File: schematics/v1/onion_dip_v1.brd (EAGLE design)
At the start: 41 x 50 mm, 28 parts

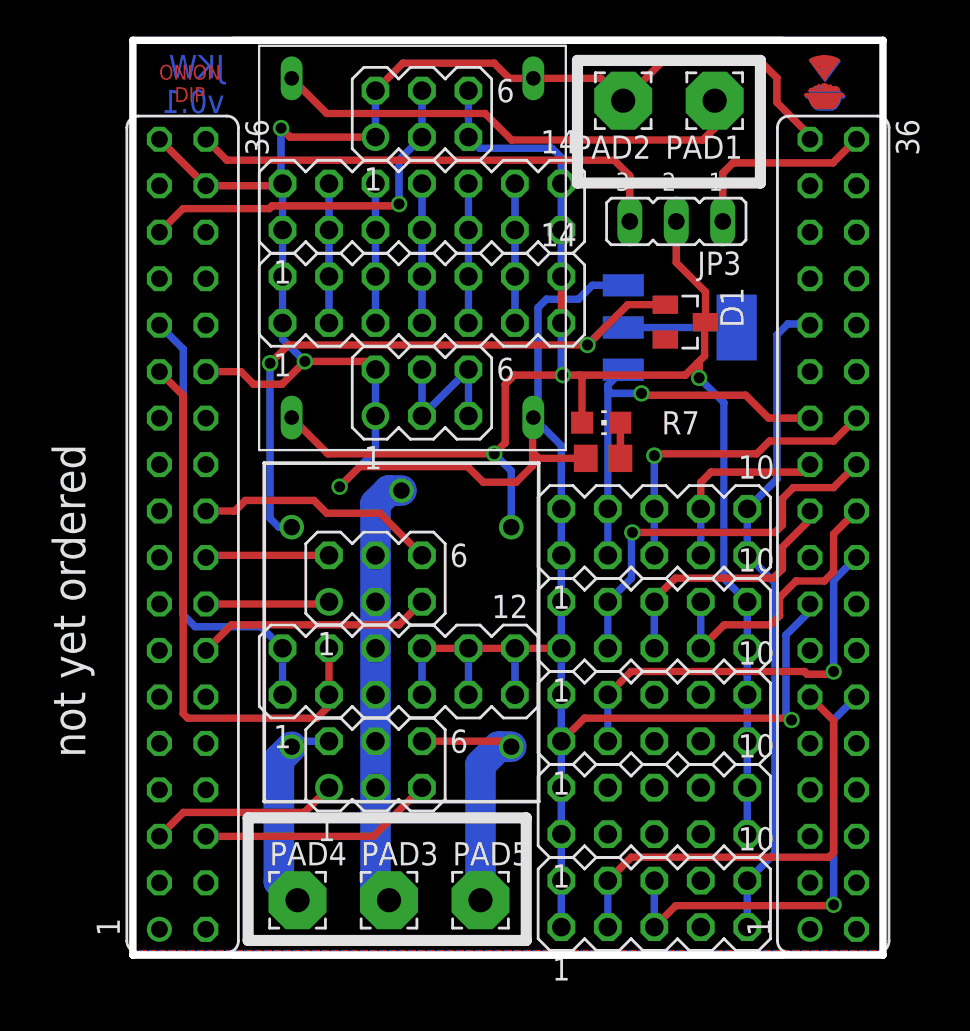
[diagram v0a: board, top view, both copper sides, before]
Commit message: added EEPROM, SPI, SMB Diode
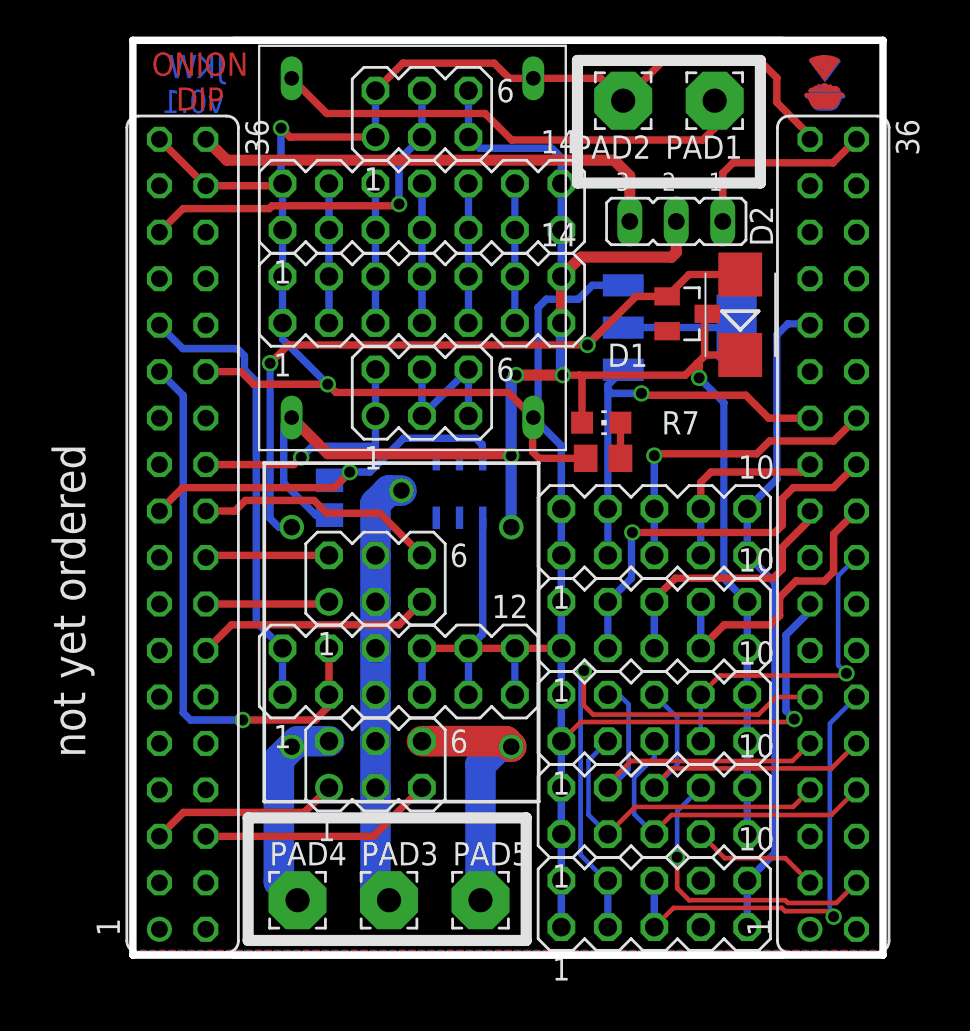
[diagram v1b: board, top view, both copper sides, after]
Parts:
- added D2: (no value), diode:SMB
- added IC2: DS2432P, 1wire:TSOC6
- added R1: (no value), rcl:R0805
- moved D1 0.46 mm to (30.3, 35.0)
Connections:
- removed net N$18: SV9.6
- removed net N$19: SV9.8
- removed net N$21: SV9.5
- removed net N$22: SV9.7
- removed net N$23: SV4.4
- removed net N$24: SV4.6
- removed net N$25: SV4.8
- removed net N$26: SV4.3
- removed net N$31: SV4.5
- removed net N$32: SV4.7
- net CSICK: now also SV4.6, SV9.6
- net CSIHSYNC: now also SV4.3, SV9.3
- net CSIPCK: now also SV4.4, SV9.4
- net CSVSYNC: now also SV4.5, SV9.5
- net D2: now also SV4.7
- net D3: now also SV4.8
- net GND: now also IC2.4; no longer SV15.1, SV15.2
- net LD2: now also IC2.3, R1.1
- net N$1: now also D2.A
- net P7: now also SV9.7, SV9.8; no longer SV9.3, SV9.4
- net VCC: now also D2.C, R1.2
- net Y2: now also SV15.1, SV15.2
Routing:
- net LD2: track 0.00 -> 21.5 mm, vias 0 -> 1
- net CSIPCK: track 0.00 -> 19.1 mm
- net CSICK: track 0.00 -> 18.2 mm
- net CSVSYNC: track 0.00 -> 18.1 mm
- net CSIHSYNC: track 0.00 -> 18.0 mm
- net D3: track 0.00 -> 16.6 mm, vias 0 -> 1
- net Y2: track 0.00 -> 13.9 mm, vias 0 -> 1
- net VCC: track 89.8 -> 101.4 mm, vias 3 -> 4
- net D2: track 0.00 -> 7.07 mm
- net SDA2: track 24.6 -> 29.7 mm, vias 0 -> 1
- net N$1: track 41.3 -> 46.1 mm
- net P7: track 22.3 -> 17.9 mm
- net GND: track 167.8 -> 166.1 mm, vias 4 -> 3
- net SCL2: track 24.7 -> 25.7 mm
- net SCK: track 30.7 -> 30.8 mm, vias 0 -> 1

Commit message: added UART header
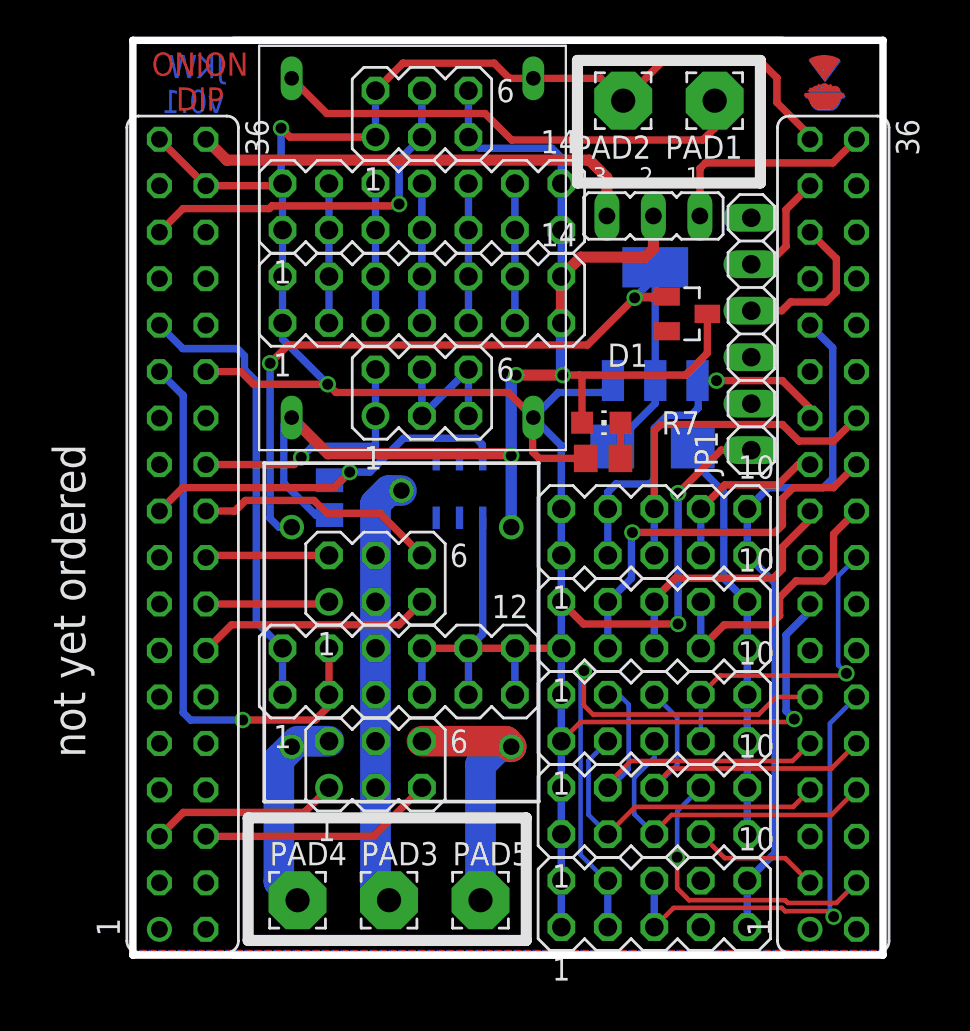
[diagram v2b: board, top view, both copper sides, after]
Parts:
- added JP1: (no value), pinhead:1X06
- moved D2 8.65 mm to (28.4, 27.8), flipped to the bottom, turned to 0 degrees
- moved U$3 1.36 mm to (28.6, 34.5), turned to 0 degrees
- moved JP3 1.29 mm to (28.4, 40.4)
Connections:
- net GND: now also JP1.1
- net RX: now also JP1.4
- net TX: now also JP1.5
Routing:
- net GND: track 166.1 -> 179.1 mm, vias 3 -> 5
- net RX: track 0.00 -> 8.93 mm
- net VCC: track 101.4 -> 94.9 mm, vias 4 -> 3
- net TX: track 0.00 -> 6.15 mm
- net _3V3: track 36.4 -> 38.4 mm
- net CHR_IN: track 26.5 -> 24.9 mm
- net P1: track 17.3 -> 18.9 mm, vias 1 -> 0
- net CHIP_5V: track 10.7 -> 12.2 mm
- net P0: track 22.2 -> 20.8 mm
- net N$1: track 46.1 -> 47.0 mm
- net P2: track 10.4 -> 9.51 mm

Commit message: new logo
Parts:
- removed U$2, U$5: LOGO, logo:LOGO
- added U$4, U$6: LOGO_3X3_COPPER, logo:LOGO_3X3_COPPER
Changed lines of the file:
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@@
 <attribute name="VALUE" x="42.979" y="0.14" size="1.27" layer="27" ratio="10" rot="R90"/>
 </element>
-<element name="U$2" library="logo" package="LOGO" value="LOGO" x="36.5379" y="46.0248"/>
-<element name="U$5" library="logo" package="LOGO" value="LOGO" x="39.0906" y="46.101" rot="MR0"/>
 <element name="PAD1" library="wirepad" package="3,17/1,3" value="WIREPAD3,17/1,3" x="31.8" y="46.7" rot="R180"/>
 <element name="PAD2" library="wirepad" package="3,17/1,3" value="WIREPAD3,17/1,3" x="26.8" y="46.7" rot="R180"/>
@@
 </element>
 <element name="JP1" library="pinhead" package="1X06" value="" x="33.8" y="33.95" rot="R90"/>
+<element name="U$4" library="logo" package="LOGO_3X3_COPPER" value="LOGO_3X3_COPPER" x="38.05" y="47.85"/>
+<element name="U$6" library="logo" package="LOGO_3X3_COPPER" value="LOGO_3X3_COPPER" x="38.05" y="47.85" rot="MR0"/>
 </elements>
 <signals>

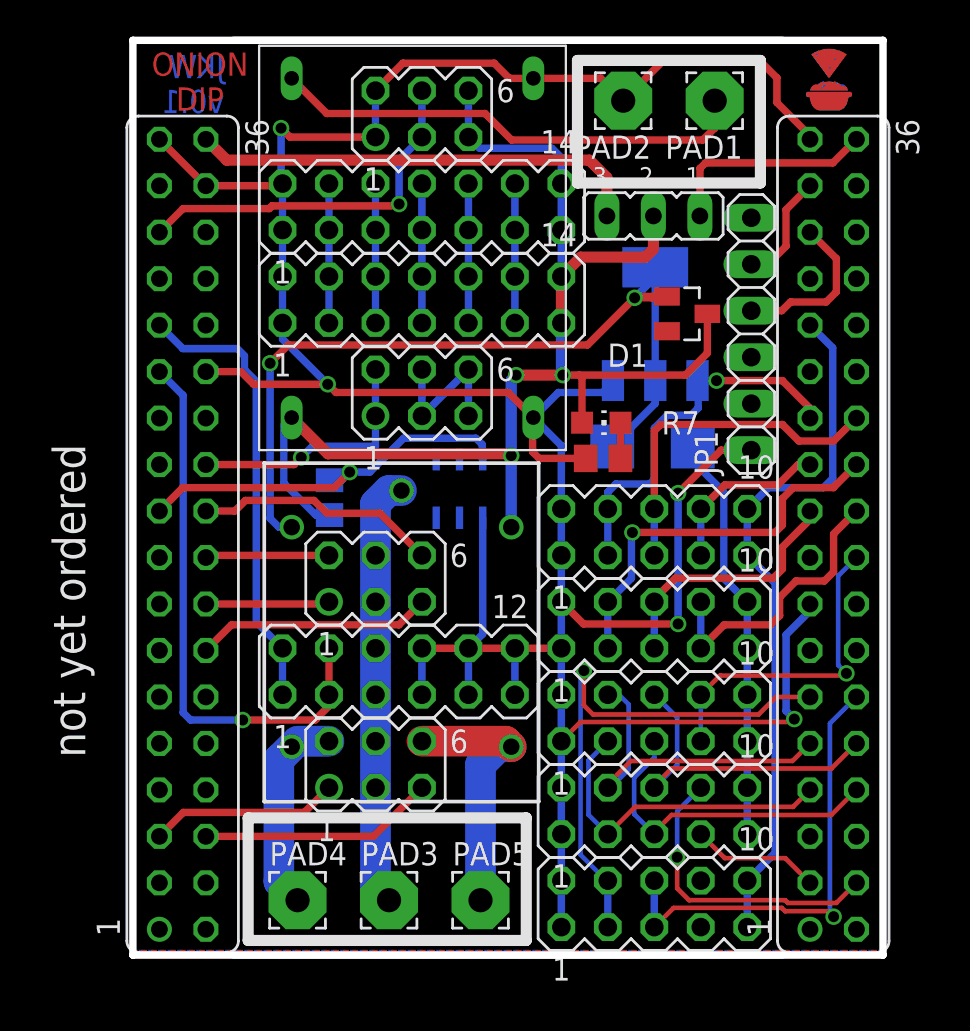
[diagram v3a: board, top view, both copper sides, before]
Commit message: add silkscreen and forum wishes
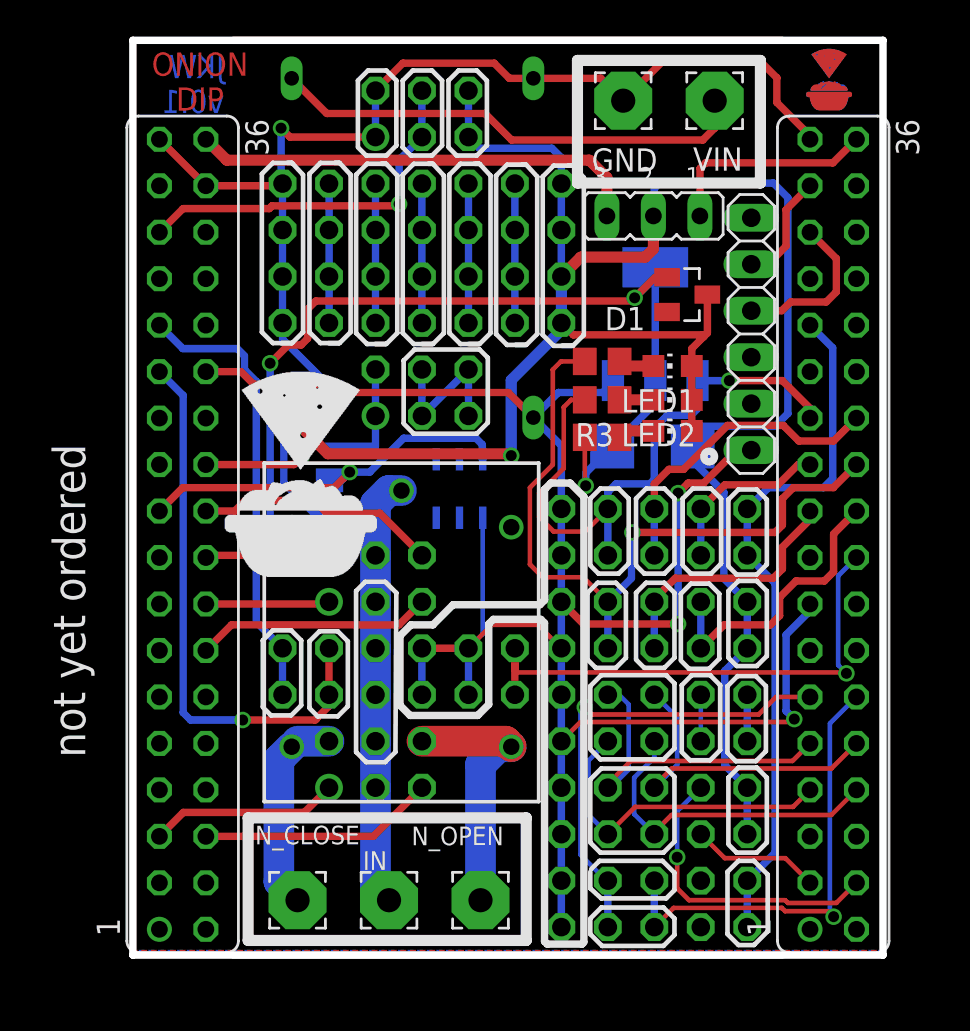
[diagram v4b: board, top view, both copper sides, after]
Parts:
- added LED1, LED2: (no value), led:CHIP-LED0805
- added R2, R3: 330R, rcl:R0805
- added U$5: LOGO_10X10_SILK, logo:LOGO_10X10_SILK
- SV1, SV10, SV11, SV4, SV9: device con-lstb:MA05-2 -> con-lstb_no_frame:MA05-2
- SV12, SV15, SV16, SV6: device con-lstb:MA03-2 -> con-lstb_no_frame:MA03-2
- SV14: device con-lstb:MA06-2 -> con-lstb_no_frame:MA06-2
- SV20, SV21: device con-lstb:MA07-2 -> con-lstb_no_frame:MA07-2
- U$9: value MP1584EN -> MP1584EN_FRAMELESS; device power_supply:MP1584EN -> power_supply:MP1584EN_FRAMELESS
- moved LED5 3.93 mm to (29.5, 28.6), turned to 90 degrees
- moved R7 1.15 mm to (25.6, 28.3)
- moved D1 1.05 mm to (30.3, 36.1)
- renumbered JP1 to ASDASD, PAD1 to VIN, PAD2 to GND, PAD3 to IN, PAD4 to N_CLOSE, PAD5 to N_OPEN
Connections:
- removed net N$1: D1.1, D2.A, U$1.COIL0, U$3.2, U$3.4
- new net N$3: LED1.C, R2.1
- new net N$4: LED2.C, R3.1
- new net N4: SV9.7, SV9.8
- new net N5: SV9.10, SV9.9
- new net RELAY_LO: D1.1, D2.A, R7.2, U$1.COIL0, U$3.2, U$3.4
- net GND: no longer R7.2, SV14.11, SV14.12
- net P0: now also R3.2
- net P3: now also R2.2
- net P7: now also SV14.11, SV14.12; no longer SV9.7, SV9.8
- net VCC: now also LED1.A, LED2.A; no longer SV9.10, SV9.9
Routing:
- net RELAY_LO: track 0.00 -> 52.9 mm, vias 0 -> 3
- net N$1: track 47.0 -> 0.00 mm, vias 2 -> 0
- net VCC: track 94.9 -> 119.4 mm, vias 3 -> 1
- net P3: track 21.5 -> 39.7 mm
- net P0: track 20.8 -> 33.3 mm
- net P7: track 17.9 -> 28.9 mm
- net GND: track 179.1 -> 172.7 mm
- net SDA2: track 29.7 -> 25.7 mm
- net N5: track 0.00 -> 2.54 mm
- net N4: track 0.00 -> 2.54 mm
- net N$3: track 0.00 -> 1.95 mm
- net N$4: track 0.00 -> 1.85 mm
- net P1: track 18.9 -> 17.6 mm

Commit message: added more pins for DIP tinker area
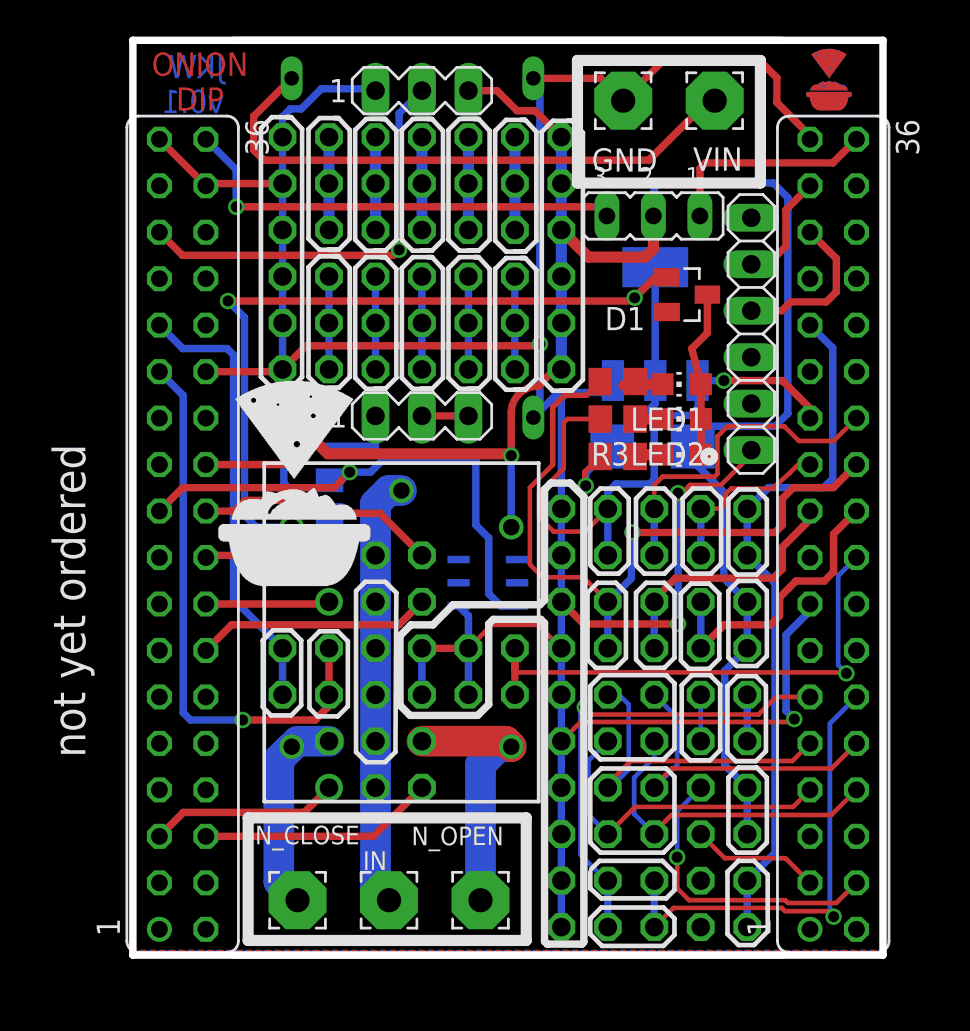
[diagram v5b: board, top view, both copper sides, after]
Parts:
- removed SV15, SV16: (no value), con-lstb_no_frame:MA03-2
- added SV5, SV8: (no value), con-lstb_no_frame:MA03-1
- added SV7: (no value), con-lstb_no_frame:MA07-2
- moved IC2 5.38 mm to (19.4, 20.4), turned to 270 degrees
- moved SV20 2.54 mm to (15.8, 43.4)
- moved SV21 2.54 mm to (15.8, 38.4)
- moved LED5 1.39 mm to (30.0, 27.4)
- moved R2 1.39 mm to (26.5, 31.4)
- moved R3 1.35 mm to (26.5, 29.3)
- moved R7 1.35 mm to (26.5, 27.2)
- moved LED2 1.16 mm to (30.0, 29.3)
- moved LED1 1.12 mm to (30.0, 31.2)
- moved U$5 0.61 mm to (4.65, 20.1)
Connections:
- new net C11: SV20.3, SV20.4, SV21.4
- new net C21: SV20.5, SV20.6, SV21.6
- new net C31: SV20.7, SV20.8, SV21.8
- new net C41: SV20.10, SV20.9, SV21.10
- new net C51: SV20.11, SV20.12, SV21.12
- net 3V3: now also SV5.2; no longer SV16.3, SV16.4
- net C1: now also SV7.3, SV7.4; no longer SV20.3, SV20.4, SV21.4
- net C2: now also SV7.5, SV7.6; no longer SV20.5, SV20.6, SV21.6
- net C3: now also SV7.7, SV7.8; no longer SV20.7, SV20.8, SV21.8
- net C4: now also SV7.10, SV7.9; no longer SV20.10, SV20.9, SV21.10
- net C5: now also SV7.11, SV7.12; no longer SV20.11, SV20.12, SV21.12
- net GND: now also SV5.1, SV7.1, SV7.2; no longer SV16.1, SV16.2
- net N$2: now also SV8.2, SV8.3; no longer SV15.3, SV15.4, SV15.5, SV15.6
- net VCC: now also SV5.3, SV7.13, SV7.14; no longer SV16.5, SV16.6
- net Y2: now also SV8.1; no longer SV15.1, SV15.2
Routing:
- net LD2: track 21.5 -> 29.2 mm
- net N$2: track 8.67 -> 2.54 mm
- net VIN: track 26.3 -> 31.6 mm
- net C51: track 0.00 -> 5.08 mm
- net C41: track 0.00 -> 5.08 mm
- net C31: track 0.00 -> 5.08 mm
- net C21: track 0.00 -> 5.08 mm
- net C11: track 0.00 -> 5.08 mm
- net RELAY_LO: track 52.9 -> 57.2 mm
- net Y2: track 13.9 -> 11.3 mm
- net C5: track 7.62 -> 5.08 mm
- net C4: track 7.62 -> 5.08 mm
- net C3: track 7.62 -> 5.08 mm
- net C2: track 7.62 -> 5.08 mm
- net C1: track 7.62 -> 5.08 mm
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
